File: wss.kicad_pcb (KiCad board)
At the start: 2 copper layers, 51 x 44 mm, 20 parts, among them J1 Conn_01x02, J2 Conn_01x02, J3 Conn_01x03, U2 TLV9061xDBV

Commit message: Add text and labels
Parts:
- added Wheel Speed Sensor (2026): LOGO, WSS:FBR_Logo_.9in, B.Cu at (121.6, 84.6)
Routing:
- net Net-(R5-Pad2): track 18.6 -> 24.6 mm

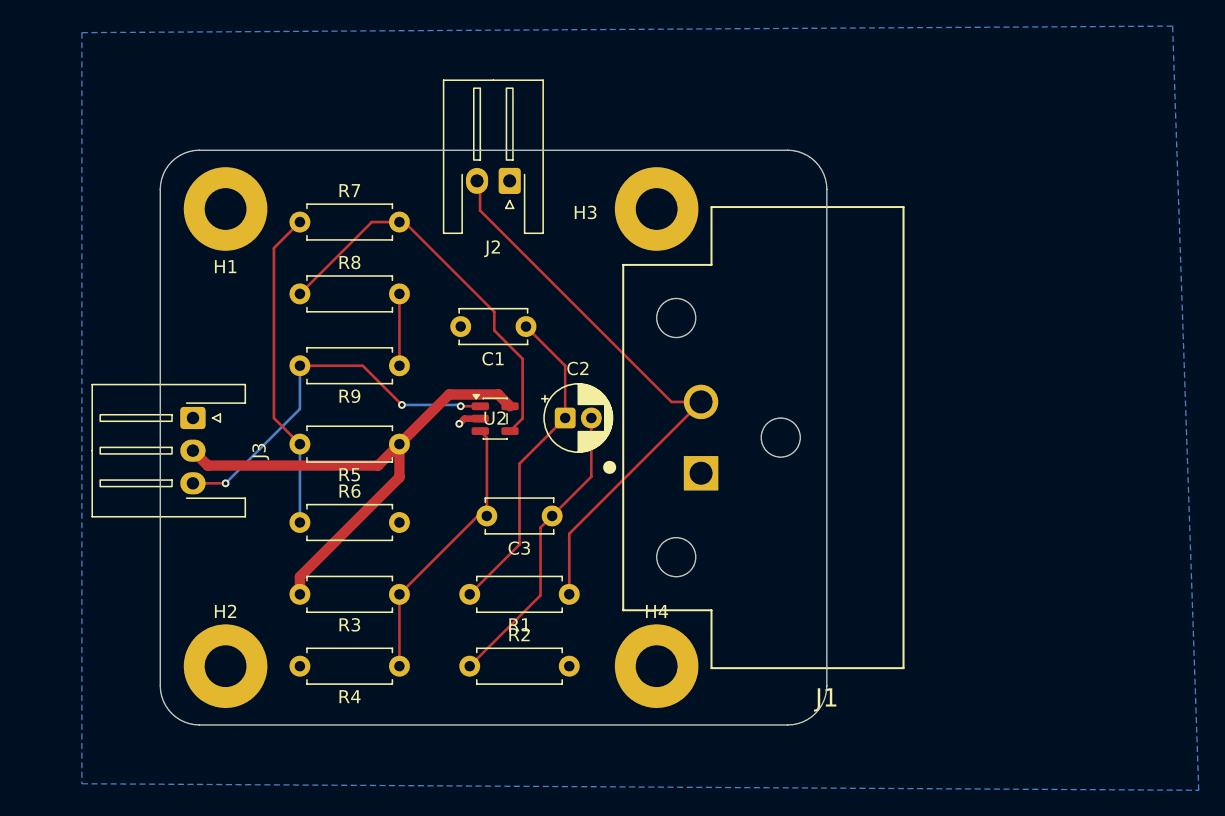
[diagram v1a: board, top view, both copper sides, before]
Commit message: added schmitt trigger comparator
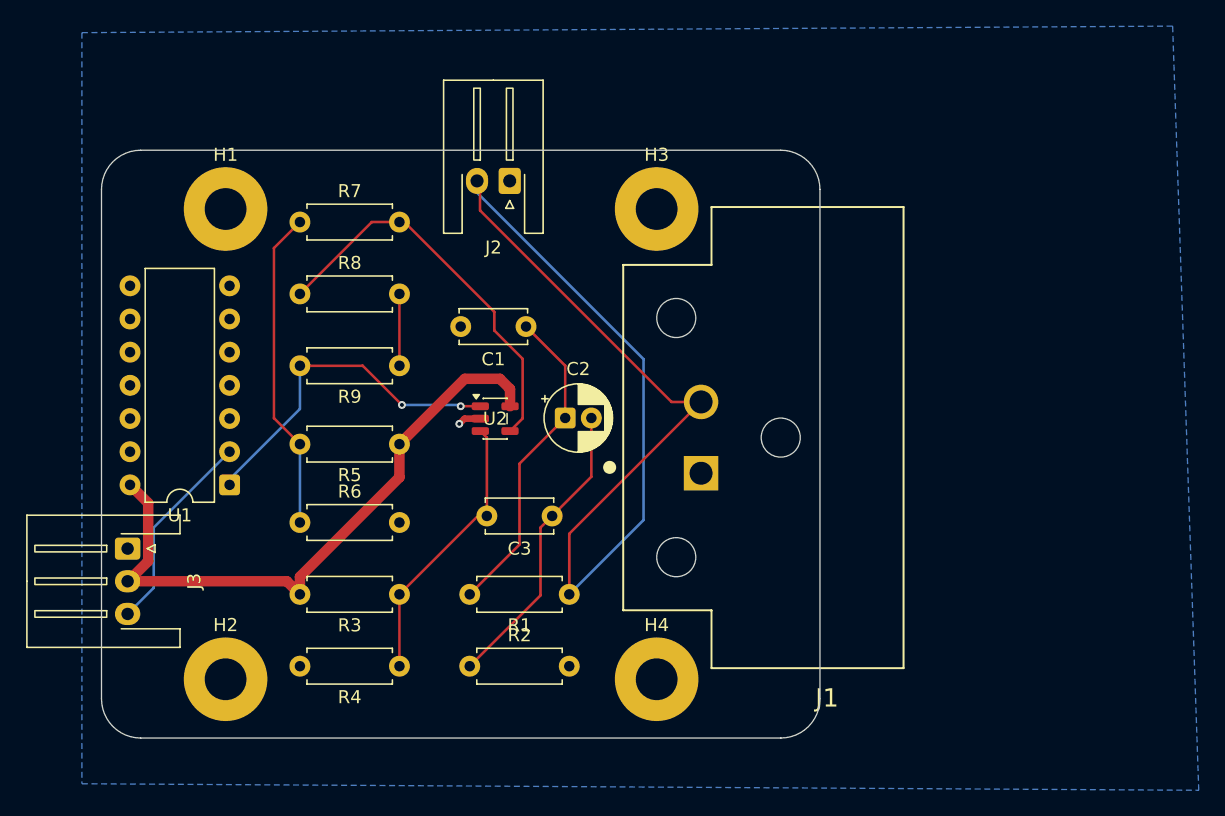
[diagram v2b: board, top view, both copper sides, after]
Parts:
- removed Wheel Speed Sensor (2026): LOGO, WSS:FBR_Logo_.9in
- added U1: 74HC14, Package_DIP:DIP-14_W7.62mm, F.Cu at (90.3, 79.6)
- R8: value 560k -> 5.6M
- moved J3 11.2 mm to (82.5, 84.5)
- moved H2 1.00 mm to (90.0, 94.5)
- moved H4 1.00 mm to (123.0, 94.5)
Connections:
- R9 pad 2: /Signal_Output -> Net-(R9-Pad2)
- U2 pad 1: /Signal_Output -> Net-(R9-Pad2)
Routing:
- net /Signal2: track 44.2 -> 83.4 mm
- net Net-(R9-Pad2): track 0.00 -> 26.4 mm, vias 0 -> 2
- net /Signal_Output: track 28.9 -> 15.7 mm, vias 3 -> 0
- net +3V3: track 42.0 -> 49.1 mm
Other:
- board size 51 x 44 mm -> 55 x 45 mm
